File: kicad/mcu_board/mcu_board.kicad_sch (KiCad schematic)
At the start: 25 parts, among them J2 Conn_02x04_Odd_Even

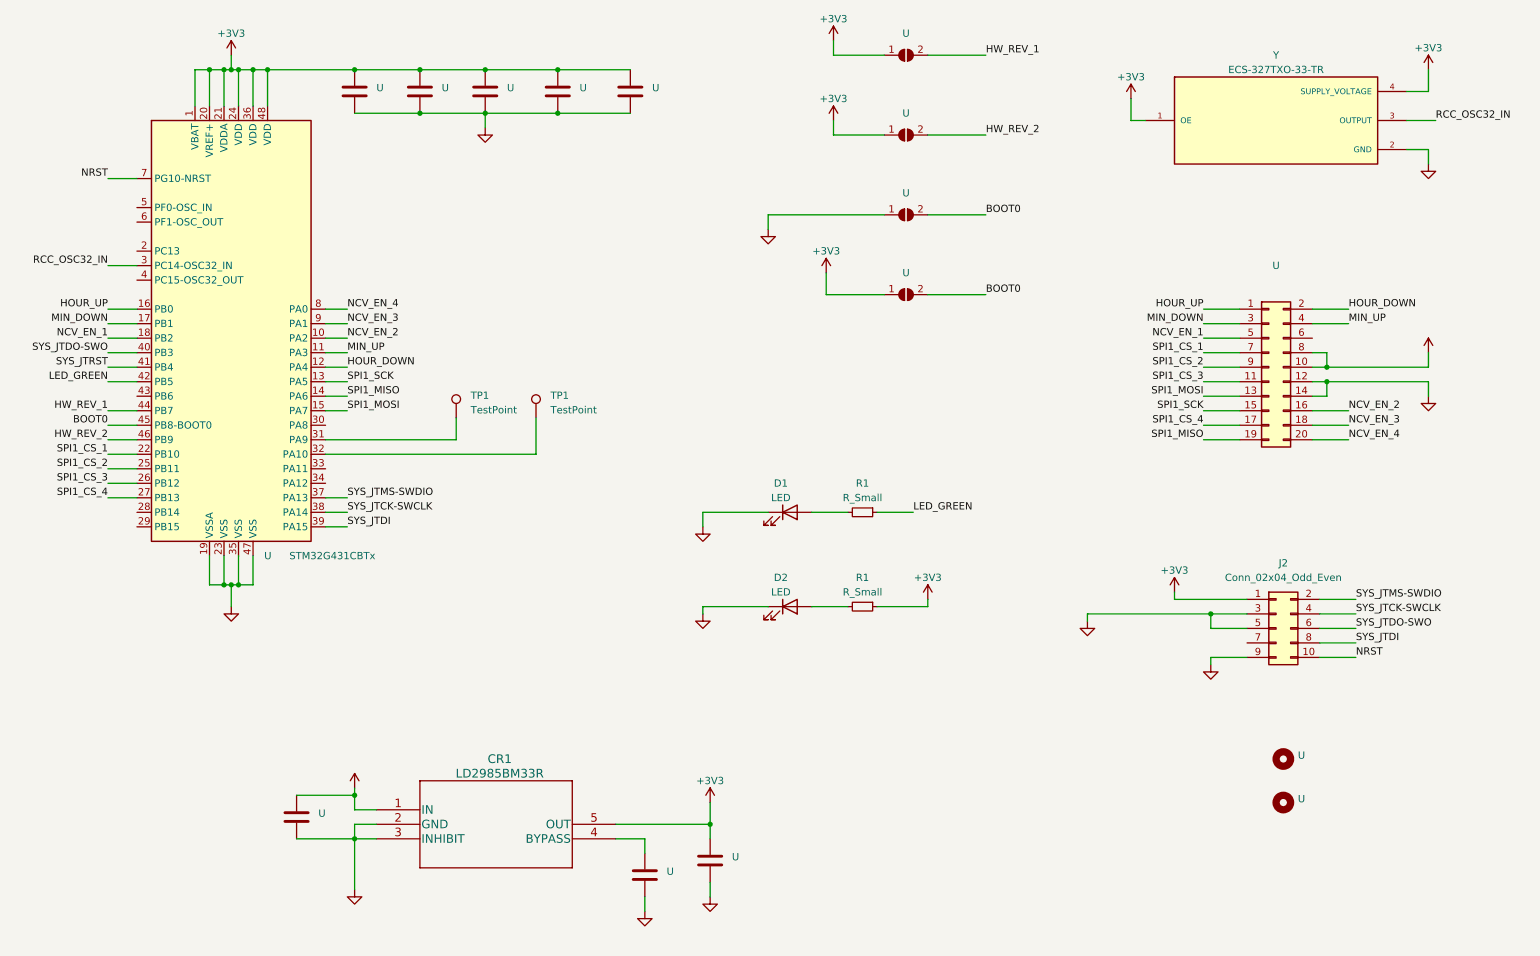
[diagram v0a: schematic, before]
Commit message: fix LDO bug. FW updates to support new HW
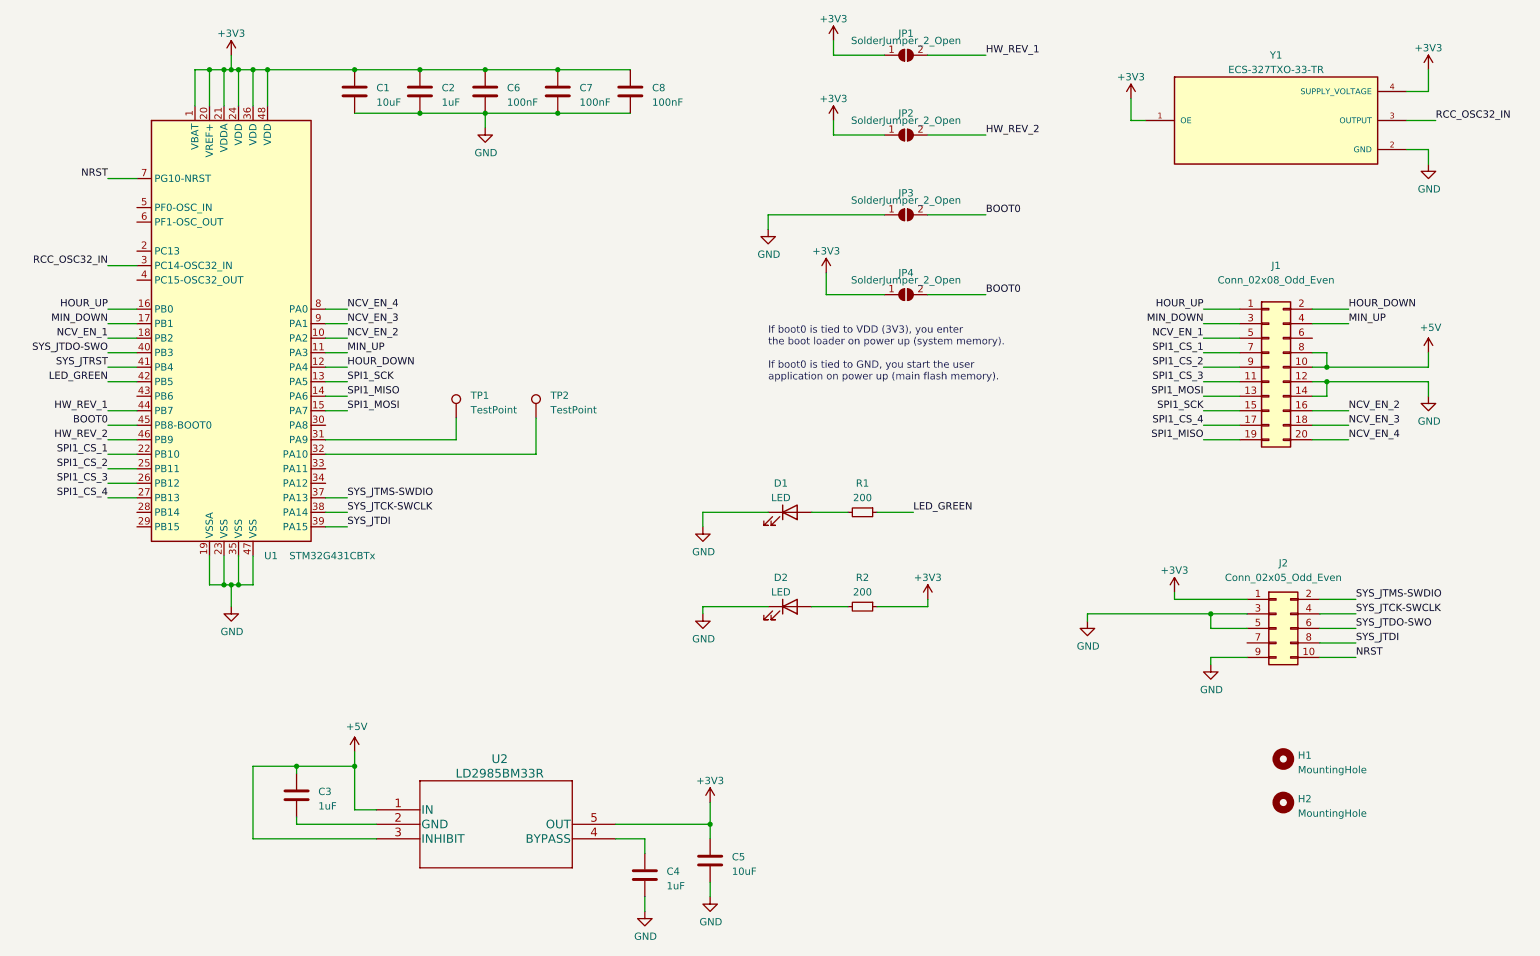
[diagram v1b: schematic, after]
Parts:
- C1, C5: renamed from U; value (none) -> 10uF; footprint (none) -> Capacitor_SMD:C_0805_2012Metric
- C2, C3, C4: renamed from U; value (none) -> 1uF; footprint (none) -> Capacitor_SMD:C_0805_2012Metric
- C6, C7, C8: renamed from U; value (none) -> 100nF; footprint (none) -> Capacitor_SMD:C_0603_1608Metric
- D1, D2: footprint (none) -> LED_SMD:LED_0603_1608Metric
- H1, H2: renamed from U; value (none) -> MountingHole; footprint (none) -> mio:MountingHole_3.2mm_M3
- J1: renamed from U; value (none) -> Conn_02x08_Odd_Even; footprint (none) -> Connector_PinHeader_2.54mm:PinHeader_2x10_P2.54mm_Vertical
- J2: value Conn_02x04_Odd_Even -> Conn_02x05_Odd_Even; footprint (none) -> Connector_PinHeader_1.27mm:PinHeader_2x05_P1.27mm_Vertical
- JP1, JP2, JP3, JP4: renamed from U; value (none) -> SolderJumper_2_Open; footprint (none) -> Jumper:SolderJumper-2_P1.3mm_Open_TrianglePad1.0x1.5mm
- R1: value R_Small -> 200; footprint (none) -> Resistor_SMD:R_0603_1608Metric
- R2: renamed from R1; value R_Small -> 200; footprint (none) -> Resistor_SMD:R_0603_1608Metric
- TP1: footprint (none) -> TestPoint:TestPoint_Pad_D1.0mm
- TP2: renamed from TP1; footprint (none) -> TestPoint:TestPoint_Pad_D1.0mm
- U2: renamed from CR1; footprint SOT23-5L_STM -> mio:SOT23-5L_STM
- Y1: renamed from Y; footprint OSC_ECS-327TXO-33-TR -> mio:ECS-327TXO-33-TR
- renumbered U to U1
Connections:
- net +5V: now also U2.3 (INHIBIT)
- net GND: no longer C3.2, U2.2 (GND), U2.3 (INHIBIT)
- new net: C3.2, U2.2 (GND)
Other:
- note added: "If boot0 is tied to VDD (3V3), you enter the boot loader on power up (system memory). If boot0 is tied to GND, you start the user application on power up (main flash memory)."
- moved on the sheet: C3

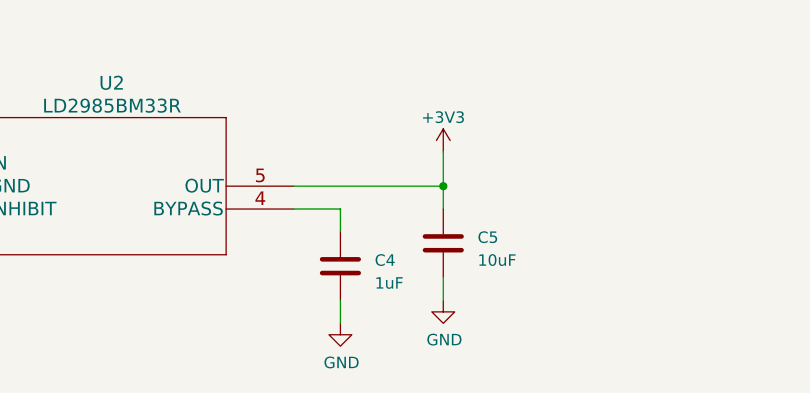
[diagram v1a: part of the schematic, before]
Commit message: use 100nF 0603 for bypass cap
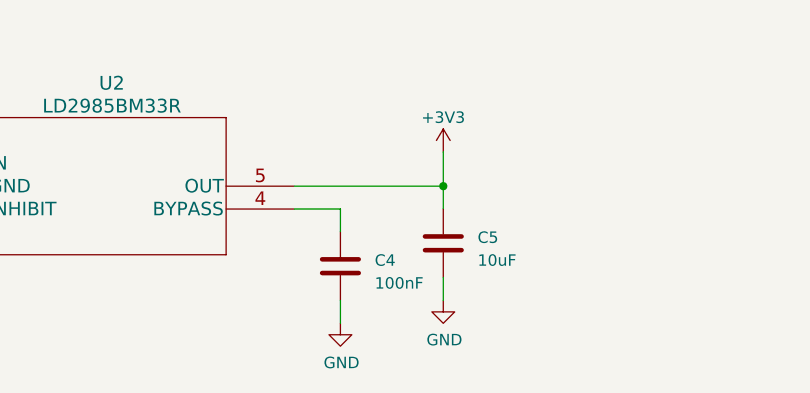
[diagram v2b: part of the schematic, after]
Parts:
- C4: value 1uF -> 100nF; footprint Capacitor_SMD:C_0805_2012Metric -> Capacitor_SMD:C_0603_1608Metric; LCSC Part Number C107367 -> C184760
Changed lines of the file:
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@@
       (effects (font (size 1.27 1.27)) (justify left))
     )
-    (property "Value" "1uF" (at 129.54 172.085 0)
+    (property "Value" "100nF" (at 129.54 172.085 0)
       (effects (font (size 1.27 1.27)) (justify left))
     )
-    (property "Footprint" "Capacitor_SMD:C_0805_2012Metric" (at 126.6952 173.99 0)
+    (property "Footprint" "Capacitor_SMD:C_0603_1608Metric" (at 126.6952 173.99 0)
       (effects (font (size 1.27 1.27)) hide)
     )
@@
       (effects (font (size 1.27 1.27)) hide)
     )
-    (property "LCSC Part Number" "C107367" (at 125.73 170.18 0)
+    (property "LCSC Part Number" "C184760" (at 125.73 170.18 0)
       (effects (font (size 1.27 1.27)) hide)
     )
@@
       (project "mcu_board"
         (path "/2faae2bb-a0c2-4054-ae9f-2d25525a48e8"
-          (reference "C4") (unit 1) (value "1uF") (footprint "Capacitor_SMD:C_0805_2012Metric")
+          (reference "C4") (unit 1) (value "100nF") (footprint "Capacitor_SMD:C_0603_1608Metric")
         )
       )

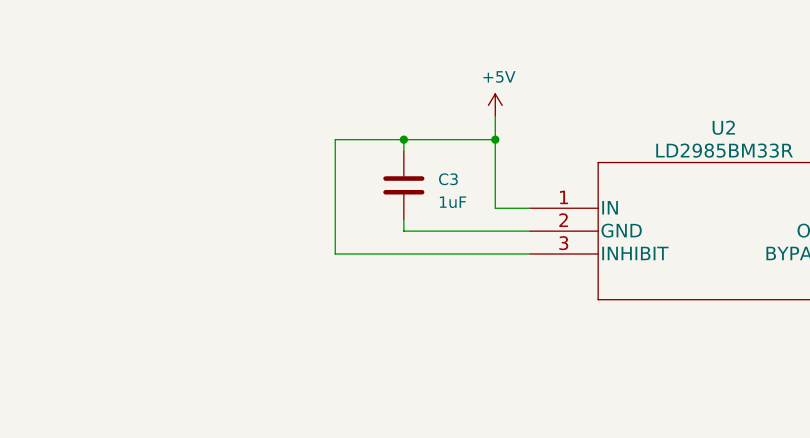
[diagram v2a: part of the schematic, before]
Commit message: rework LDO section
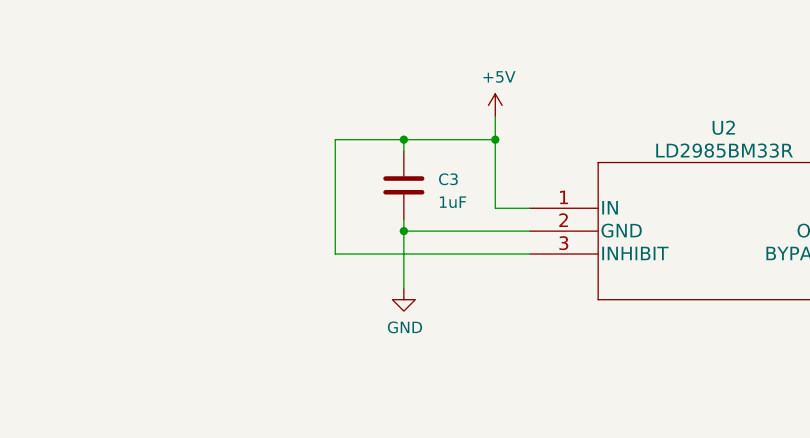
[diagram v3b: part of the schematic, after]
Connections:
- net GND: now also C3.2, U2.2 (GND)
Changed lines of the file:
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@@
   (junction (at 64.77 151.13) (diameter 0) (color 0 0 0 0)
   )
+  (junction (at 64.77 161.29) (diameter 0) (color 0 0 0 0)
+  )
   (junction (at 52.07 29.21) (diameter 0) (color 0 0 0 0)
   )
@@
   )
   (wire (pts (xy 223.52 78.74) (xy 229.87 78.74))
+    (stroke (width 0) (type default))
+  )
+  (wire (pts (xy 64.77 161.29) (xy 64.77 167.64))
     (stroke (width 0) (type default))
   )
@@
         )
       )
+    )
+  )
+  (symbol (lib_id "power:GND") (at 64.77 167.64 0) (unit 1)
+    (in_bom yes) (on_board yes) (dnp no)
+    (property "Reference" "#PWR0117" (at 64.77 173.99 0)
+      (effects (font (size 1.27 1.27)) hide)
+    )
+    (property "Value" "GND" (at 64.897 172.0342 0)
+      (effects (font (size 1.27 1.27)))
+    )
+    (property "Footprint" "" (at 64.77 167.64 0)
+      (effects (font (size 1.27 1.27)) hide)
+    )
+    (property "Datasheet" "" (at 64.77 167.64 0)
+      (effects (font (size 1.27 1.27)) hide)
+    )
+    (pin "1")
+    (instances
+      (project "mcu_board"
+        (path "/2faae2bb-a0c2-4054-ae9f-2d25525a48e8"
+          (reference "#PWR0117") (unit 1) (value "GND") (footprint "")
+        )
+      )

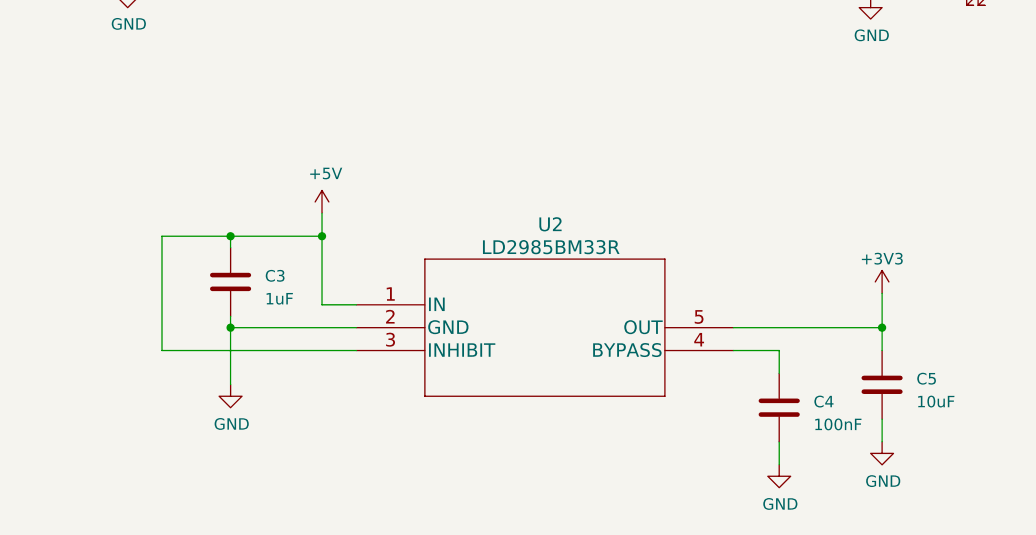
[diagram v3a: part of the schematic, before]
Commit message: layout update for LDO
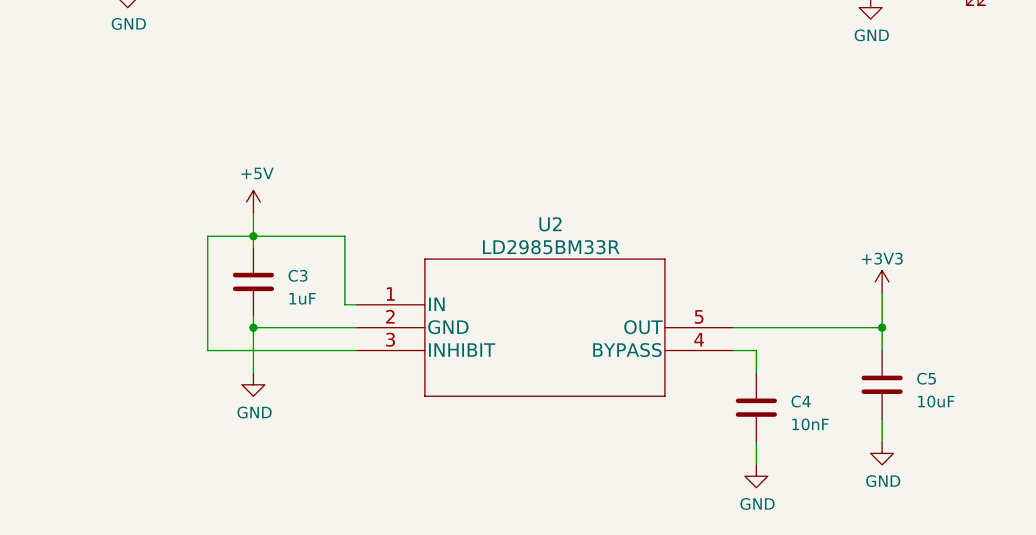
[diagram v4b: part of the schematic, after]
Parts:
- C4: value 100nF -> 10nF; LCSC Part Number C184760 -> C519405
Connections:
- net +5V: now also C3.2; no longer C3.1
- net GND: now also C3.1, C4.1; no longer C3.2, C4.2
- net at U2.4 (BYPASS): now also C4.2; no longer C4.1
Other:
- moved on the sheet: C3, C4

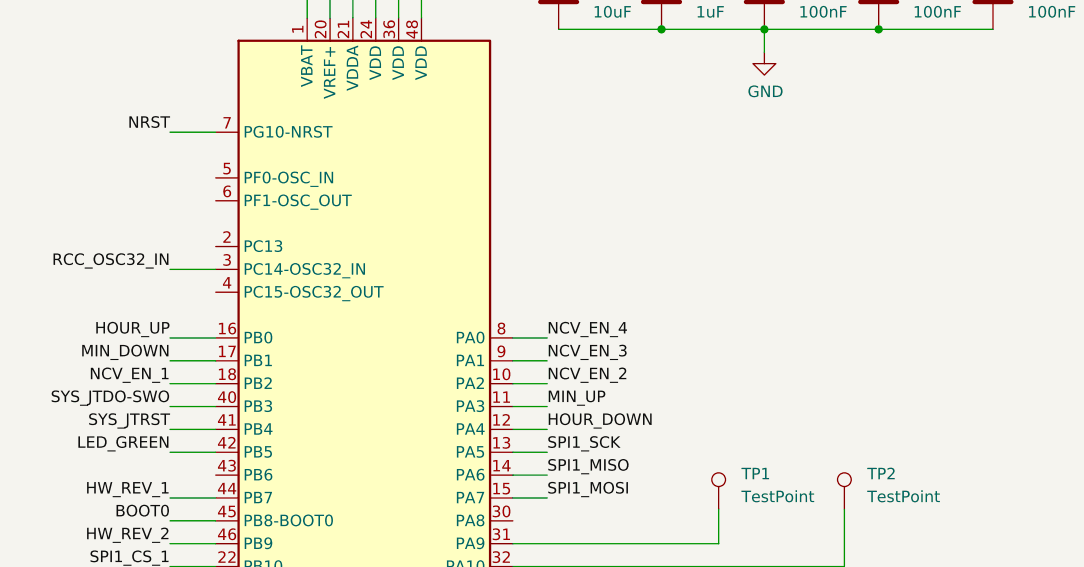
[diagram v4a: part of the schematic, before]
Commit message: LSCO output on PA2
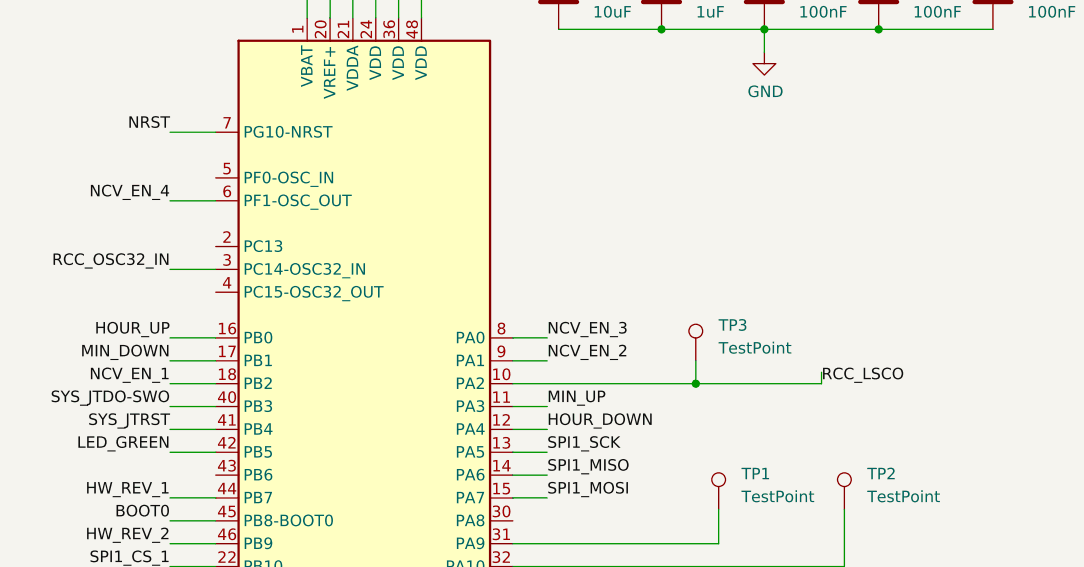
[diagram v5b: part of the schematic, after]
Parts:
- added TP3: TestPoint, TestPoint:TestPoint_Pad_D1.0mm, symbol Connector:TestPoint
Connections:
- net NCV_EN_2: now also U1.9 (PA1); no longer U1.10 (PA2)
- net NCV_EN_3: now also U1.8 (PA0); no longer U1.9 (PA1)
- net NCV_EN_4: now also U1.6 (PF1-OSC_OUT); no longer U1.8 (PA0)
- new net RCC_LSCO: TP3.1, U1.10 (PA2)
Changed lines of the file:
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@@
   (junction (at 54.61 119.38) (diameter 0) (color 0 0 0 0)
   )
+  (junction (at 90.17 76.2) (diameter 0) (color 0 0 0 0)
+  )
   (junction (at 110.49 29.21) (diameter 0) (color 0 0 0 0)
   )
@@
     (stroke (width 0) (type default))
   )
+  (wire (pts (xy 104.14 76.2) (xy 104.14 74.93))
+    (stroke (width 0) (type default))
+  )
   (wire (pts (xy 106.68 96.52) (xy 106.68 90.17))
     (stroke (width 0) (type default))
@@
     (stroke (width 0) (type default))
   )
-  (wire (pts (xy 69.85 76.2) (xy 73.66 76.2))
+  (wire (pts (xy 69.85 76.2) (xy 90.17 76.2))
+    (stroke (width 0) (type default))
+  )
+  (wire (pts (xy 90.17 73.66) (xy 90.17 76.2))
     (stroke (width 0) (type default))
   )
@@
     (stroke (width 0) (type default))
   )
+  (wire (pts (xy 31.75 55.88) (xy 36.83 55.88))
+    (stroke (width 0) (type default))
+  )
   (wire (pts (xy 245.11 86.36) (xy 245.11 83.82))
     (stroke (width 0) (type default))
@@
   )
   (wire (pts (xy 67.31 161.29) (xy 67.31 160.02))
+    (stroke (width 0) (type default))
+  )
+  (wire (pts (xy 90.17 76.2) (xy 104.14 76.2))
     (stroke (width 0) (type default))
   )
@@
     (effects (font (size 1.27 1.27)) (justify left bottom))
   )
-  (label "NCV_EN_3" (at 73.66 73.66 0) (fields_autoplaced)
-    (effects (font (size 1.27 1.27)) (justify left bottom))
-  )
   (label "SYS_JTMS-SWDIO" (at 73.66 104.14 0) (fields_autoplaced)
     (effects (font (size 1.27 1.27)) (justify left bottom))
@@
     (effects (font (size 1.27 1.27)) (justify left bottom))
   )
+  (label "NCV_EN_2" (at 73.66 73.66 0) (fields_autoplaced)
+    (effects (font (size 1.27 1.27)) (justify left bottom))
+  )
   (label "RCC_OSC32_IN" (at 264.16 38.1 0) (fields_autoplaced)
     (effects (font (size 1.27 1.27)) (justify left bottom))
@@
     (effects (font (size 1.27 1.27)) (justify right bottom))
   )
+  (label "NCV_EN_4" (at 31.75 55.88 180) (fields_autoplaced)
+    (effects (font (size 1.27 1.27)) (justify right bottom))
+  )
   (label "HW_REV_1" (at 31.75 88.9 180) (fields_autoplaced)
     (effects (font (size 1.27 1.27)) (justify right bottom))
@@
     (effects (font (size 1.27 1.27)) (justify left bottom))
   )
-  (label "NCV_EN_4" (at 73.66 71.12 0) (fields_autoplaced)
-    (effects (font (size 1.27 1.27)) (justify left bottom))
-  )
   (label "SYS_JTRST" (at 31.75 81.28 180) (fields_autoplaced)
     (effects (font (size 1.27 1.27)) (justify right bottom))
@@
     (effects (font (size 1.27 1.27)) (justify left bottom))
   )
+  (label "RCC_LSCO" (at 104.14 76.2 0) (fields_autoplaced)
+    (effects (font (size 1.27 1.27)) (justify left bottom))
+  )
   (label "NCV_EN_1" (at 223.52 76.2 0) (fields_autoplaced)
     (effects (font (size 1.27 1.27)) (justify right bottom))
@@
     (effects (font (size 1.27 1.27)) (justify right bottom))
   )
-  (label "NCV_EN_2" (at 73.66 76.2 0) (fields_autoplaced)
-    (effects (font (size 1.27 1.27)) (justify left bottom))
-  )
   (label "SPI1_CS_1" (at 223.52 78.74 0) (fields_autoplaced)
     (effects (font (size 1.27 1.27)) (justify right bottom))
+  )
+  (label "NCV_EN_3" (at 73.66 71.12 0) (fields_autoplaced)
+    (effects (font (size 1.27 1.27)) (justify left bottom))
   )
   (label "NCV_EN_1" (at 31.75 76.2 0) (fields_autoplaced)
@@
         )
       )
+    )
+  )
+  (symbol (lib_id "Connector:TestPoint") (at 90.17 73.66 0) (unit 1)
+    (in_bom no) (on_board yes) (dnp no) (fields_autoplaced)
+    (property "Reference" "TP3" (at 92.71 69.723 0)
+      (effects (font (size 1.27 1.27)) (justify left))
+    )
+    (property "Value" "TestPoint" (at 92.71 72.263 0)
+      (effects (font (size 1.27 1.27)) (justify left))
+    )
+    (property "Footprint" "TestPoint:TestPoint_Pad_D1.0mm" (at 95.25 73.66 0)
+      (effects (font (size 1.27 1.27)) hide)
+    )
+    (property "Datasheet" "~" (at 95.25 73.66 0)
+      (effects (font (size 1.27 1.27)) hide)
+    )
+    (pin "1")
+    (instances
+      (project "mcu_board"
+        (path "/2faae2bb-a0c2-4054-ae9f-2d25525a48e8"
+          (reference "TP3") (unit 1) (value "TestPoint") (footprint "TestPoint:TestPoint_Pad_D1.0mm")
+        )
+      )
